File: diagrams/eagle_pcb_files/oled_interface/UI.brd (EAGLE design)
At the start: 33.8 x 50.8 mm, 19 parts, among them Q1 BCX59SMD, Q2 BCX59SMD

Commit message: make routing in UI more home-made-possible
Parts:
- R1, R2, R3, R5, R6: value (none) -> 10k
- R4: value (none) -> 10R
- R7: value (none) -> 200R
- moved R7 1.56 mm to (46.9, -1.96)
- moved LED2 1.41 mm to (38.9, 2.18)
- moved R4 0.77 mm to (37.2, 21.8)
- renumbered U$1 to OLED
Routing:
- net GND: track 0.00 -> 65.8 mm, vias 0 -> 2
- net B1: track 37.5 -> 43.2 mm
- net N$2: track 14.8 -> 18.3 mm
- net SCL: track 21.3 -> 18.3 mm
- net N$1: track 21.2 -> 24.1 mm
- net VCC: track 77.6 -> 79.9 mm
- net BUZ: track 7.65 -> 5.41 mm
- net N$3: track 15.9 -> 14.3 mm
- net N$9: track 11.2 -> 12.5 mm
- net SDA: track 34.7 -> 33.8 mm
- net B2: track 40.2 -> 39.3 mm
- net LED: track 12.3 -> 13.0 mm

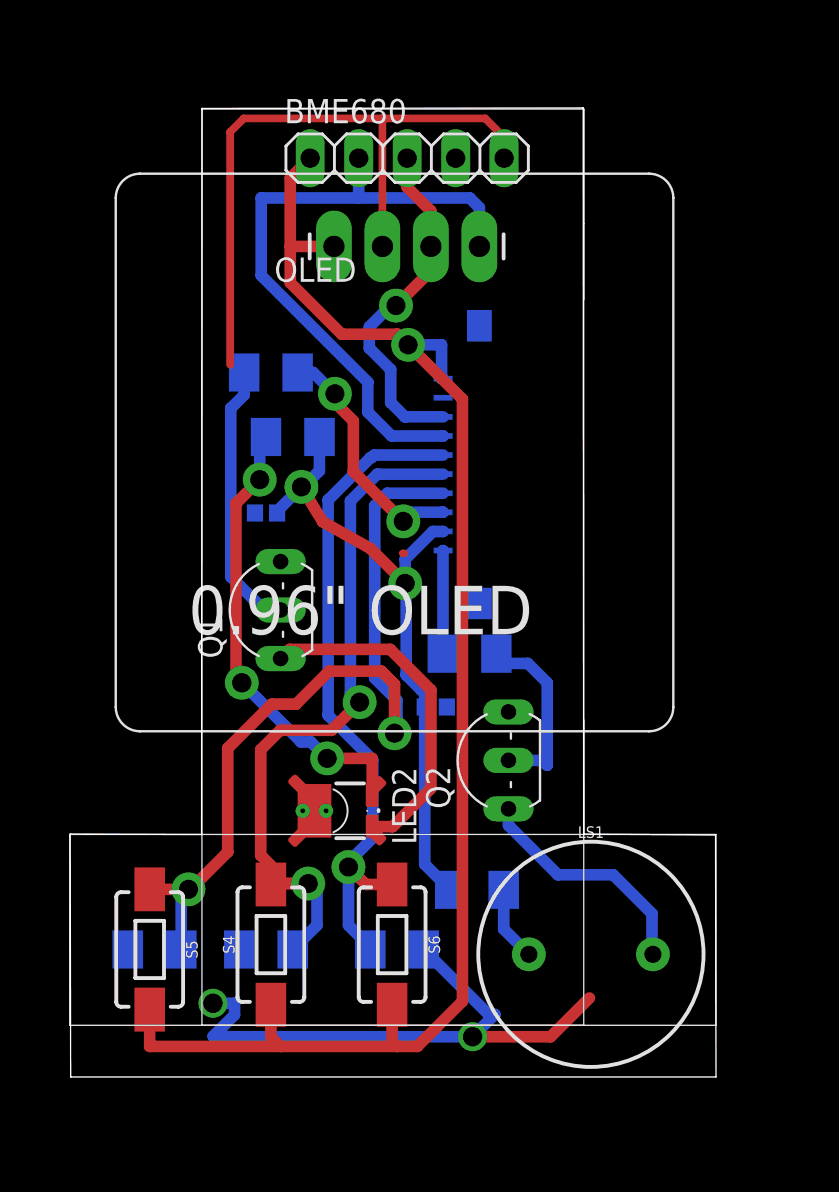
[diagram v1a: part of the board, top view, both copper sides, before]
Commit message: oled ready for production
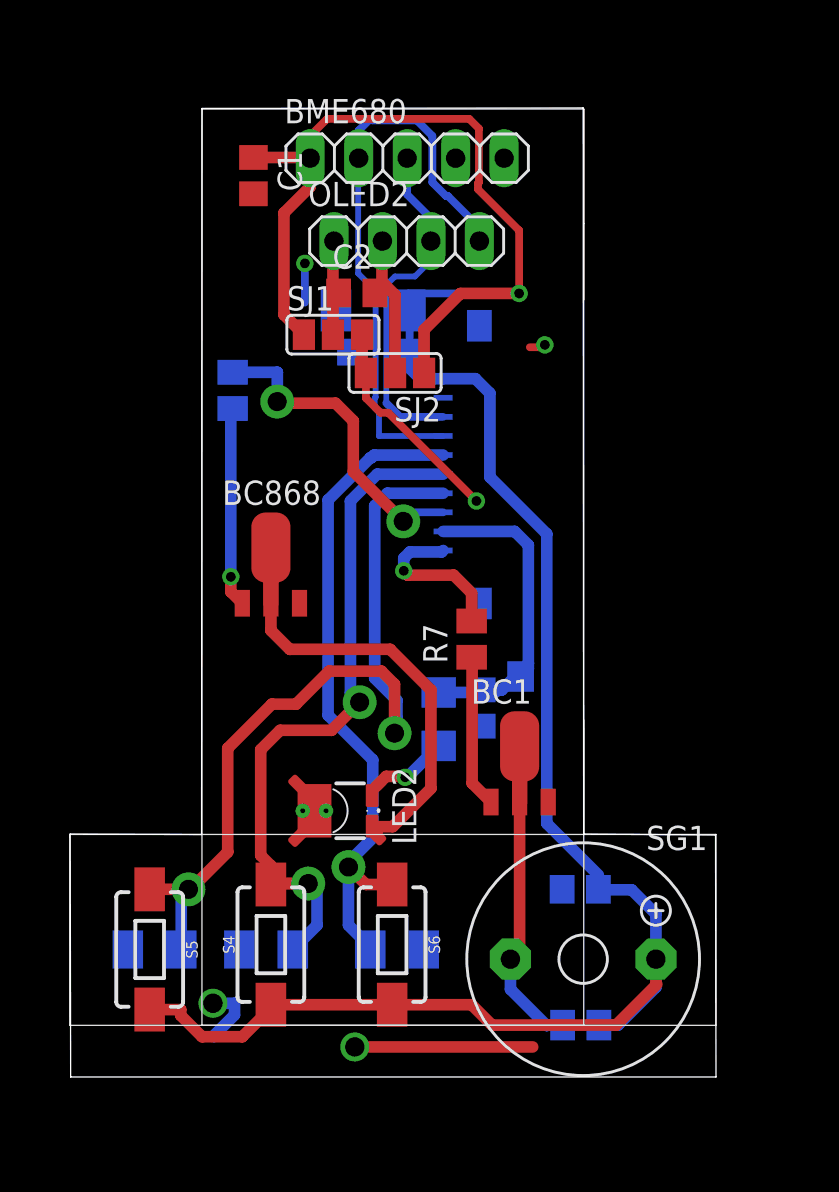
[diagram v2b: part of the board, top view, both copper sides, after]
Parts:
- removed LS1: BUZZER-PTH, SparkFun-Electromechanical:BUZZER-12MM
- removed OLED: I2C_OLED, DIYMall_OLED:I2C_OLED_PACKAGE
- removed Q1, Q2: BCX59SMD, transistor-npn:TO92-EBC
- removed R6: 10k, rcl:M1206
- added BC1, BC868: (no value), transistor:SOT89-BCE
- added C3, C7: 100nF, rcl:C0805
- added C4: 100nF, rcl:C1808
- added C5, C6: 10uF, rcl:SMC_A
- added OLED2: (no value), pinhead:1X04
- added R8: 1R, eagle-ltspice:R3216
- added SG1: F/TMB, buzzer:F/TMB
- added SJ1, SJ2: (no value), jumper:SJ_2
- C1, C2: value (none) -> 100nF; device SparkFun-Capacitors:0402 -> rcl:C0805
- R4: value 10R -> 1k; device rcl:M1206 -> rcl:M0805
- R5: value 10k -> 200R; device rcl:M1206 -> rcl:M0805
- R7: device rcl:M1206 -> rcl:M0805
- moved R4 34.3 mm to (52.3, -9.04)
- moved C1 29.4 mm to (35.2, 35.5), flipped to the top, turned to 270 degrees
- moved R7 13.1 mm to (46.6, 11.2), flipped to the top, turned to 90 degrees
- moved C2 12.5 mm to (40.6, 29.3), flipped to the top, turned to 0 degrees
- moved R5 2.22 mm to (34.1, 24.2), turned to 270 degrees
- renumbered J1 to OUT
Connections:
- removed net N$9: LS1.+, Q2.C
- removed net TH: LED2.TH, LED2.TH@1, LED2.TH@2, LED2.TH@3, LED2.TH@4
- removed net VIN1: C1.2, C2.2, OUT.9, R4.2, R7.2
- new net P1: C2.1, OLED2.1, SJ1.2
- new net P2: C2.2, OLED2.2, SJ2.2
- new net VIN: C6.+, C7.1, OUT.9, R8.2
- net BUZ: now also R7.2; no longer R6.1
- net GND: now also BC1.E, BC868.E, C1.2, C3.2, C4.2, C5.-, C6.-, C7.2, LED2.TH, LED2.TH@1, LED2.TH@2, LED2.TH@3, LED2.TH@4, SJ1.3, SJ2.3; no longer C1.1, C2.1, OLED.2, Q1.E, Q2.E
- net N$1: now also R8.1; no longer R4.1
- net N$2: now also BC868.C; no longer Q1.C
- net N$3: now also BC868.B; no longer Q1.B
- net N$7: now also BC1.B, R7.1; no longer Q2.B, R6.2
- net N$8: now also BC1.C, R4.1, SG1.-; no longer LS1.-, R7.1
- net SCL: now also OLED2.3; no longer OLED.3
- net SDA: now also OLED2.4; no longer OLED.4
- net VCC: now also C1.1, C3.1, C4.1, C5.+, R4.2, SG1.+, SJ1.1, SJ2.1; no longer OLED.1
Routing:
- net VCC: track 79.9 -> 126.4 mm
- net GND: track 65.8 -> 27.3 mm, vias 2 -> 5
- net VIN1: track 33.5 -> 0.00 mm, vias 2 -> 0
- net N$1: track 24.1 -> 4.15 mm, vias 3 -> 1
- net VIN: track 0.00 -> 18.0 mm
- net N$9: track 12.5 -> 0.00 mm
- net N$8: track 3.92 -> 13.8 mm
- net P2: track 0.00 -> 7.94 mm
- net P1: track 0.00 -> 5.27 mm
- net LED: track 13.0 -> 16.9 mm
- net N$3: track 14.3 -> 10.5 mm, vias 0 -> 1
- net BUZ: track 5.41 -> 8.41 mm, vias 0 -> 1
- net SDA: track 33.8 -> 31.0 mm
- net N$2: track 18.3 -> 20.7 mm
- net N$7: track 9.75 -> 8.00 mm
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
